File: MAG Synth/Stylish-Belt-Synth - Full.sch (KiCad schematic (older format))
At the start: 38 parts, among them J0 USB_B, J1 Headphone, J26 WRITE PATCH, J27 PARAM SELECT, J28 PATCH SELECT, J29 MODE, J30 STYLUS, U1 stm32f103c8t6-module-china, U2 XPT8871

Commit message: Changed LED ring resistor from 44Ω to 30Ω.
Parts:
- R3: value 44Ω -> 30Ω
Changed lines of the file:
@@
 P 4000 6150
 F 0 "R3" V 3900 6150 50  0000 C CNN
-F 1 "44Ω" V 4000 6150 50  0000 C CNN
+F 1 "30Ω" V 4000 6150 50  0000 C CNN
 F 2 "SoftEggKiCAD:R_Axial_DIN0204_L3.6mm_D1.6mm_P7.62mm_Horizontal+SMD804" V 3930 6150 50  0001 C CNN
 F 3 "~" H 4000 6150 50  0001 C CNN

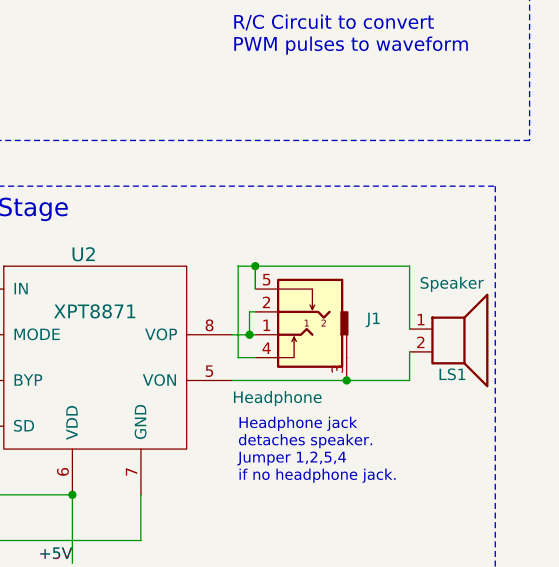
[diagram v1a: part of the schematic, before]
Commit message: Noted value of speaker in Schematic
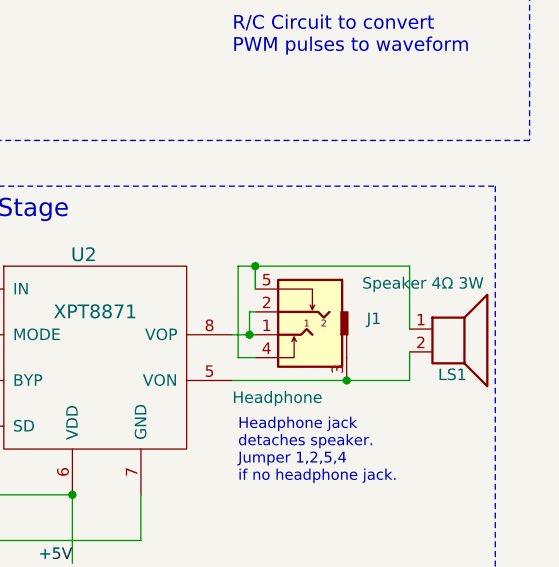
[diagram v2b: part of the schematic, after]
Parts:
- LS1: value Speaker -> Speaker 4Ω 3W
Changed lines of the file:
@@
 P 10750 5275
 F 0 "LS1" H 10800 5075 50  0000 R CNN
-F 1 "Speaker" H 10875 5475 50  0000 R CNN
+F 1 "Speaker 4Ω 3W" H 10875 5475 50  0000 R CNN
 F 2 "Pin_Headers:Pin_Header_Straight_1x02_Pitch2.54mm" H 10750 5075 50  0001 C CNN
 F 3 "" H 10740 5225 50  0001 C CNN
